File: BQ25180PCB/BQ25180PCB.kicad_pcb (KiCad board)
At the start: 2 copper layers, 7 parts, among them J1 Conn_01x04_Socket, J2 Conn_01x06_Socket, U1 BQ25180

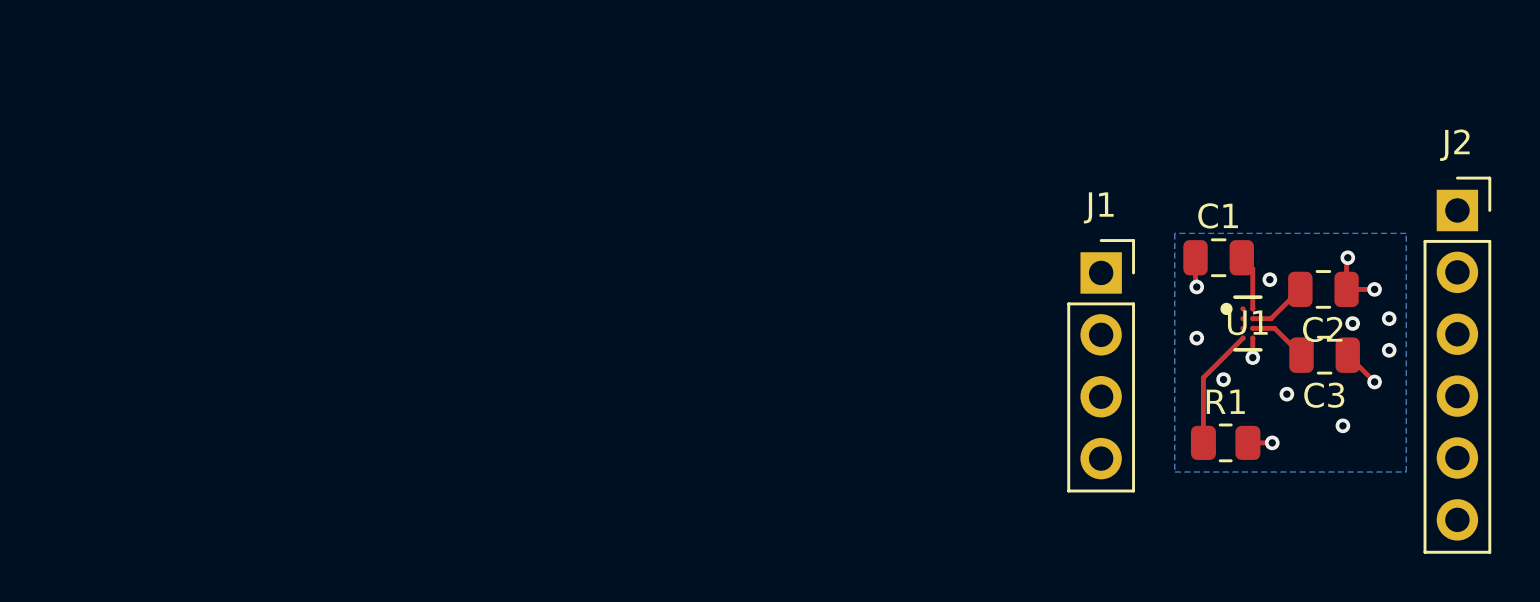
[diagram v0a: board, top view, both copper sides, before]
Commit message: bq25180 basic pcb layout
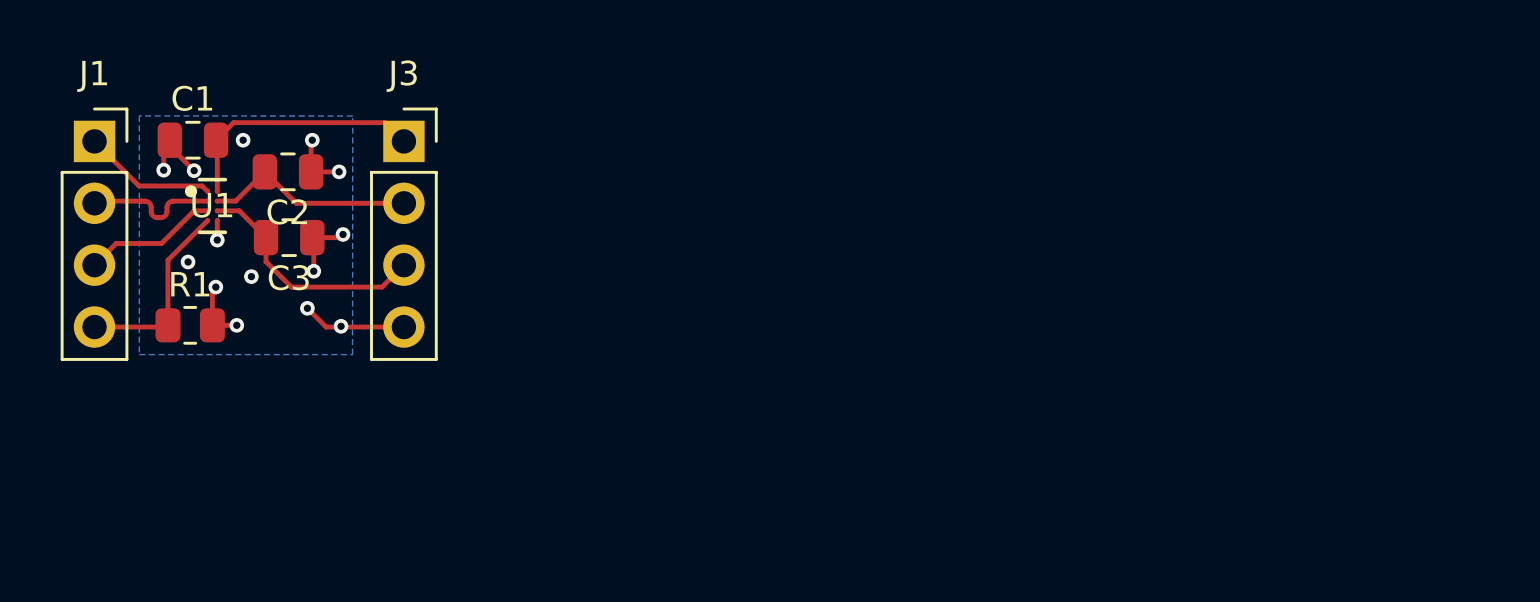
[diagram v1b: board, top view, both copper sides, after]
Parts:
- removed J2: Conn_01x06_Socket, Connector_PinSocket_2.54mm:PinSocket_1x06_P2.54mm_Vertical
- added J3: Conn_01x04_Socket, Connector_PinSocket_2.54mm:PinSocket_1x04_P2.54mm_Vertical, F.Cu at (39.4, 21.0)
- moved R1 42.8 mm to (30.6, 28.6)
- moved C3 42.8 mm to (34.6, 25.0)
- moved C2 42.8 mm to (34.6, 22.3)
- moved U1 42.8 mm to (31.5, 23.7)
- moved C1 42.4 mm to (30.7, 21.0)
- moved J1 41.7 mm to (26.7, 21.0)
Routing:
- net GND_CHRG: track 7.15 -> 16.1 mm
- net VBUS_CHRG: track 2.29 -> 10.4 mm
- net BAT_CHRG: track 2.46 -> 9.91 mm
- net SYS_CHRG: track 2.45 -> 8.69 mm
- net SDA_CHRG: track 0.00 -> 5.56 mm
- net SCL_CHRG: track 0.00 -> 5.55 mm
- net INT_CHRG: track 0.00 -> 5.49 mm
- net TS_MR_CHRG: track 4.97 -> 8.02 mm

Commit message: silkscreen
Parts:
- moved R1 0.45 mm to (30.6, 29.0)
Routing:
- net GND_CHRG: track 16.1 -> 15.4 mm, vias 14 -> 11
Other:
- board outline added: 16.4 x 11.3 mm
- board text added: "BAT"
- board text added: "GND"
- board text added: "IN"
- board text added: "INT"
- board text added: "SCL"
- board text added: "SDA"
- board text added: "SYS"
- board text added: "TSMR"
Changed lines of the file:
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@@
 		(tags "capacitor")
 		(property "Reference" "C2"
-			(at 0 -1.68 360)
-			(layer "F.SilkS")
-			(effects
-				(font
-					(size 1 1)
-					(thickness 0.15)
+			(at -0.055 1.465 0)
+			(layer "F.SilkS")
+			(effects
+				(font
+					(size 0.8 0.8)
+					(thickness 0.125)
 				)
 			)
@@
 		(tags "PQ25180YBGT ")
 		(property "Reference" "U1"
-			(at 0 0 0)
-			(unlocked yes)
-			(layer "F.SilkS")
-			(effects
-				(font
-					(size 1 1)
-					(thickness 0.15)
+			(at 0.515 2.285 0)
+			(unlocked yes)
+			(layer "F.SilkS")
+			(effects
+				(font
+					(size 0.8 0.8)
+					(thickness 0.125)
 				)
 			)
@@
 	(footprint "Resistor_SMD:R_0805_2012Metric"
 		(layer "F.Cu")
-		(at 30.5825 28.575)
+		(at 30.58 29.02)
 		(descr "Resistor SMD 0805 (2012 Metric), square (rectangular) end terminal, IPC_7351 nominal, (Body size source: IPC-SM-782 page 72, https://www.pcb-3d.com/wordpress/wp-content/uploads/ipc-sm-782a_amendment_1_and_2.pdf), generated with kicad-footprint-generator")
 		(tags "resistor")
 		(property "Reference" "R1"
-			(at 0 -1.65 0)
-			(layer "F.SilkS")
-			(effects
-				(font
-					(size 1 1)
-					(thickness 0.15)
+			(at 2.43 0.58 0)
+			(layer "F.SilkS")
+			(effects
+				(font
+					(size 0.8 0.8)
+					(thickness 0.125)
 				)
 			)
@@
 			(at 0 -2.77 0)
 			(layer "F.SilkS")
+			(hide yes)
 			(effects
 				(font
@@
 		(tags "capacitor")
 		(property "Reference" "C1"
-			(at 0 -1.68 0)
-			(layer "F.SilkS")
-			(effects
-				(font
-					(size 1 1)
-					(thickness 0.15)
+			(at 2.505 -1.205 0)
+			(layer "F.SilkS")
+			(effects
+				(font
+					(size 0.8 0.8)
+					(thickness 0.125)
 				)
 			)
@@
 		(tags "capacitor")
 		(property "Reference" "C3"
-			(at 0 -1.68 360)
-			(layer "F.SilkS")
-			(effects
-				(font
-					(size 1 1)
-					(thickness 0.15)
+			(at 0.455 -1.535 0)
+			(layer "F.SilkS")
+			(effects
+				(font
+					(size 0.8 0.8)
+					(thickness 0.125)
 				)
 			)
@@
 			(at 0 -2.77 0)
 			(layer "F.SilkS")
+			(hide yes)
 			(effects
 				(font
@@
 		)
 	)
+	(gr_rect
+		(start 24.8 19.17)
+		(end 41.16 30.48)
+		(stroke
+			(width 0.05)
+			(type default)
+		)
+		(fill none)
+		(layer "Edge.Cuts")
+	)
+	(gr_text "IN"
+		(at 36.66 21.48 0)
+		(layer "F.SilkS")
+		(effects
+			(font
+				(size 0.8 0.8)
+				(thickness 0.125)
+			)
+			(justify left bottom)
+		)
+	)
+	(gr_text "INT"
+		(at 29.07 22.24 90)
+		(layer "F.SilkS")
+		(effects
+			(font
+				(size 0.8 0.8)
+				(thickness 0.125)
+			)
+			(justify left bottom)
+		)
+	)
+	(gr_text "BAT"
+		(at 35.78 26.99 0)
+		(layer "F.SilkS")
+		(effects
+			(font
+				(size 0.8 0.8)
+				(thickness 0.125)
+			)
+			(justify left bottom)
+		)
+	)
+	(gr_text "TSMR"
+		(at 28.22 27.62 0)
+		(layer "F.SilkS")
+		(effects
+			(font
+				(size 0.8 0.8)
+				(thickness 0.125)
+			)
+			(justify left bottom)
+		)
+	)
+	(gr_text "SCL"
+		(at 28.08 24.02 0)
+		(layer "F.SilkS")
+		(effects
+			(font
+				(size 0.8 0.8)
+				(thickness 0.125)
+			)
+			(justify left bottom)
+		)
+	)
+	(gr_text "SYS"
+		(at 37.85 24.51 90)
+		(layer "F.SilkS")
+		(effects
+			(font
+				(size 0.8 0.8)
+				(thickness 0.125)
+			)
+			(justify left bottom)
+		)
+	)
+	(gr_text "SDA"
+		(at 28.08 26.57 0)
+		(layer "F.SilkS")
+		(effects
+			(font
+				(size 0.8 0.8)
+				(thickness 0.125)
+			)
+			(justify left bottom)
+		)
+	)
+	(gr_text "GND"
+		(at 35.34 30.01 0)
+		(layer "F.SilkS")
+		(effects
+			(font
+				(size 0.8 0.8)
+				(thickness 0.125)
+			)
+			(justify left bottom)
+		)
+	)
 	(segment
 		(start 39.355 21.025)
@@
 	)
 	(segment
+		(start 31.67 27.71)
+		(end 31.495 27.885)
+		(width 0.2)
+		(layer "F.Cu")
+		(net 2)
+	)
+	(segment
 		(start 36.695 22.275)
 		(end 36.595 22.275)
@@
 	)
 	(segment
-		(start 31.635 27.005)
-		(end 31.495 27.145)
-		(width 0.2)
-		(layer "F.Cu")
-		(net 2)
-	)
-	(segment
 		(start 36.725 24.975)
 		(end 36.855 24.845)
@@
 	)
 	(segment
-		(start 31.495 27.145)
-		(end 31.495 28.575)
-		(width 0.2)
-		(layer "F.Cu")
-		(net 2)
-	)
-	(segment
 		(start 36.165 28.645)
 		(end 35.395 27.875)
@@
 	)
 	(segment
+		(start 29.495 22.205)
+		(end 29.495 21.225)
+		(width 0.2)
+		(layer "F.Cu")
+		(net 2)
+	)
+	(segment
 		(start 31.495 28.575)
 		(end 32.495 28.575)
@@
 	)
 	(segment
-		(start 29.495 22.205)
-		(end 29.495 21.225)
-		(width 0.2)
-		(layer "F.Cu")
-		(net 2)
-	)
-	(segment
 		(start 29.495 21.225)
 		(end 29.745 20.975)
+		(width 0.2)
+		(layer "F.Cu")
+		(net 2)
+	)
+	(segment
+		(start 31.495 27.885)
+		(end 31.495 28.575)
 		(width 0.2)
 		(layer "F.Cu")
@@
 	)
 	(via
-		(at 32.755 20.975)
-		(size 0.6)
-		(drill 0.3)
-		(layers "F.Cu" "B.Cu")
-		(free yes)
-		(net 2)
-	)
-	(via
 		(at 36.695 22.275)
 		(size 0.6)
@@
 		(drill 0.3)
 		(layers "F.Cu" "B.Cu")
-		(net 2)
-	)
-	(via
-		(at 30.495 25.975)
-		(size 0.6)
-		(drill 0.3)
-		(layers "F.Cu" "B.Cu")
-		(free yes)
-		(net 2)
-	)
-	(via
-		(at 33.095 26.575)
-		(size 0.6)
-		(drill 0.3)
-		(layers "F.Cu" "B.Cu")
-		(free yes)
 		(net 2)
 	)
@@
 	)
 	(via
-		(at 31.635 27.005)
+		(at 31.67 27.71)
 		(size 0.6)
 		(drill 0.3)

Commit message: jlcpcb files
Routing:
- net GND_CHRG: track 15.4 -> 14.1 mm, vias 11 -> 9
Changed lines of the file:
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@@
+			)
+		)
+		(property "LCSC" "C3682423"
+			(at 0 0 0)
+			(unlocked yes)
+			(layer "F.Fab")
+			(hide yes)
+			(effects
+				(font
+					(size 1 1)
+					(thickness 0.15)
+				)
 			)
 		)
@@
 	)
 	(segment
-		(start 39.355 28.645)
-		(end 36.805 28.645)
-		(width 0.2)
-		(layer "F.Cu")
-		(net 2)
-	)
-	(segment
-		(start 36.745 28.645)
-		(end 36.165 28.645)
-		(width 0.2)
-		(layer "F.Cu")
-		(net 2)
-	)
-	(segment
 		(start 35.545 22.275)
 		(end 35.545 21.025)
@@
 	)
 	(segment
-		(start 36.805 28.645)
-		(end 36.775 28.615)
-		(width 0.2)
-		(layer "F.Cu")
-		(net 2)
-	)
-	(segment
 		(start 29.745 21.225)
 		(end 29.745 20.975)
-		(width 0.2)
-		(layer "F.Cu")
-		(net 2)
-	)
-	(segment
-		(start 36.775 28.615)
-		(end 36.745 28.645)
-		(width 0.2)
-		(layer "F.Cu")
-		(net 2)
-	)
-	(segment
-		(start 36.165 28.645)
-		(end 35.395 27.875)
 		(width 0.2)
 		(layer "F.Cu")
@@
 	)
 	(via
-		(at 35.395 27.875)
-		(size 0.6)
-		(drill 0.3)
-		(layers "F.Cu" "B.Cu")
-		(free yes)
-		(net 2)
-	)
-	(via
-		(at 36.775 28.615)
-		(size 0.6)
-		(drill 0.3)
-		(layers "F.Cu" "B.Cu")
-		(net 2)
-	)
-	(via
 		(at 36.855 24.845)
 		(size 0.6)
@@
 		(net 2)
 	)
+	(segment
+		(start 39.355 28.645)
+		(end 36.585 28.645)
+		(width 1)
+		(layer "B.Cu")
+		(net 2)
+	)
+	(segment
+		(start 36.585 28.645)
+		(end 36.41 28.47)
+		(width 1)
+		(layer "B.Cu")
+		(net 2)
+	)
